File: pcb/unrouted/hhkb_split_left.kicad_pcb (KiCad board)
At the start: 4 copper layers, 140.4 x 97.4 mm, 67 parts, among them SW1 Esc, SW10 E, SW11 R, SW12 T, SW13 Ctrl, SW14 A, SW15 S, SW16 D, SW17 F, SW18 G, SW19 Shift, SW2 1, SW20 Z, SW21 X, SW22 C, SW23 V, SW24 B, SW25 Alt, SW26 Meta, SW27 L-Space, SW3 2, SW4 3, SW5 4, SW6 5, SW7 Tab, SW8 Q, SW9 W, U1 74HC595

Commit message: スイッチ→ダイオードを自分で引き、ビアを 4〜5 割減らした
自動配線器が数 mm の接続のために内層へ往復し、SW*_D だけで左 30 個・
右 62 個のビアを使っていた（右が多いのは列のバスが 9 本あって裏面が
混むため）。ソケットの端子とダイオードのアノードは同じ x に並べてあり
（DIODE_OFFSET はそのために選んだ値）、裏面の L 字 2 本で届く。
**経路に選択の余地が無い**ので prewire_switch_diode で自分で引き、
GND と同じく DSN からネットごと外して (type protect) で渡す。

  ビア 左 68→40 / 右 111→51   総長 左 1574→1538 / 右 1940→1902mm
  左右の比 1.28 がキー数の比 1.26 とほぼ一致し、非対称が規模差だけで
  説明できるようになった。DRC は 0/0 のまま

FFC が子基板まで届くかの検査を足した。J_DB を左 9.1mm・右 8.5mm
動かしたのに、それを見る検査が無かった（ケーブルは発注品なので、
合わないと分かるのが組み立て時になる）。左 92.1mm / 右 78.5mm 要り、
100mm で足りる。FFC_LENGTH / FFC_SLACK は暫定値として登録。
左右で同じケーブルが使えることも見る（部品表を 2 種類にしない）。

検査を書く途中で test_pcb.footprints() が信用できないと分かった。
`.*?` で最初の (at ...) を拾うため、J_DB では左が誤った座標・右が空を
返す。この検査では括弧の対応で切り出す _footprint_blocks を使った。

Co-Authored-By: Claude Opus 5 <noreply@anthropic.com>
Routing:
- net SW4_D: track 0.00 -> 6.89 mm
- net SW22_D: track 0.00 -> 6.89 mm
- net SW6_D: track 0.00 -> 6.89 mm
- net SW5_D: track 0.00 -> 6.89 mm
- net SW3_D: track 0.00 -> 6.89 mm
- net SW2_D: track 0.00 -> 6.89 mm
- net SW1_D: track 0.00 -> 6.89 mm
- net SW9_D: track 0.00 -> 6.89 mm
- net SW8_D: track 0.00 -> 6.89 mm
- net SW7_D: track 0.00 -> 6.89 mm
- net SW24_D: track 0.00 -> 6.89 mm
- net SW23_D: track 0.00 -> 6.89 mm
- net SW21_D: track 0.00 -> 6.89 mm
- net SW20_D: track 0.00 -> 6.89 mm
- net SW19_D: track 0.00 -> 6.89 mm
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
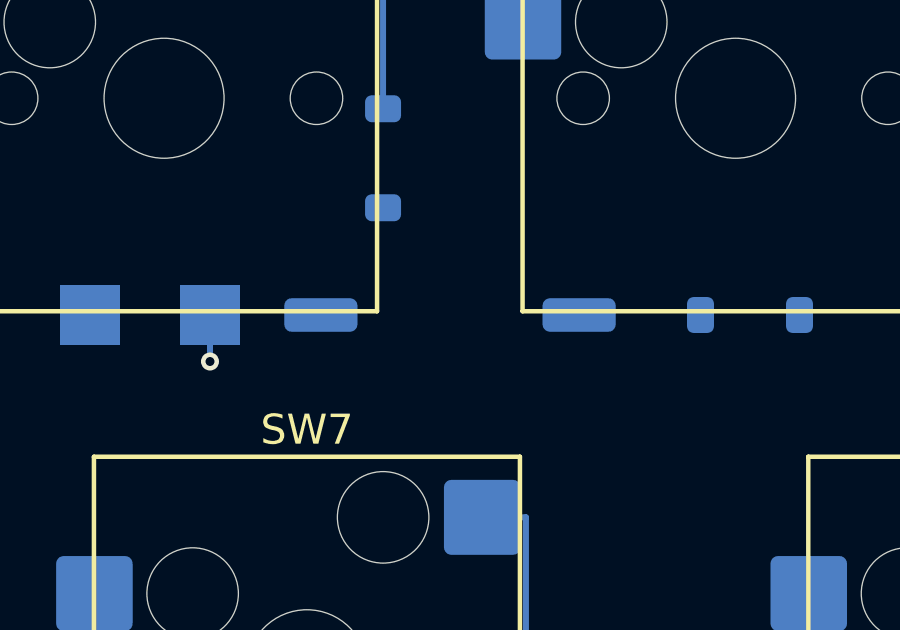
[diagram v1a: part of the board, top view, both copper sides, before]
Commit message: 電源スイッチを基板から外し、背面パネルへ（open-gaps #17 解決）
基板の後端からケース背面まで 23.3mm あり、基板の上のどこに置いても
背面には出せない。「基板に載せる」という前提自体が誤りだった。

SW_PWR の種類を wire_pads にし、基板は SW_PWR_1 / SW_PWR_2 の
ランド 2 個で受ける。電池ボックスと同じ形。実物は背面パネルに付けて
配線で繋ぐ。部品はプッシュロック（オルタネート）の丸ボタン
（実機の「電源／Bluetooth ペアリング」も丸ボタン。機械接点なので
電池を本当に切り離せる）。

再発防止に test_no_user_operated_part_is_sealed_inside を追加。
故意にスイッチを基板へ戻すと落ちることを確認済み。**最初に書いた版は
空振りしていた**（配線済み基板を読むのに再生成しか走らせておらず、
検査対象が変わっていなかった）。配線まで通して確かめ直した。

ランド 2 個への展開規則を circuit.board_refs に一本化した。
gen_pcb と test_pcb と test_conformance が別々に「battery_holder だけ
2 個」と持っていたため、電源スイッチを変えた瞬間に検査 6 件が落ちた。

検査 260 件通過。DRC は 3 基板とも 0/0 のまま。

Co-Authored-By: Claude Opus 5 <noreply@anthropic.com>
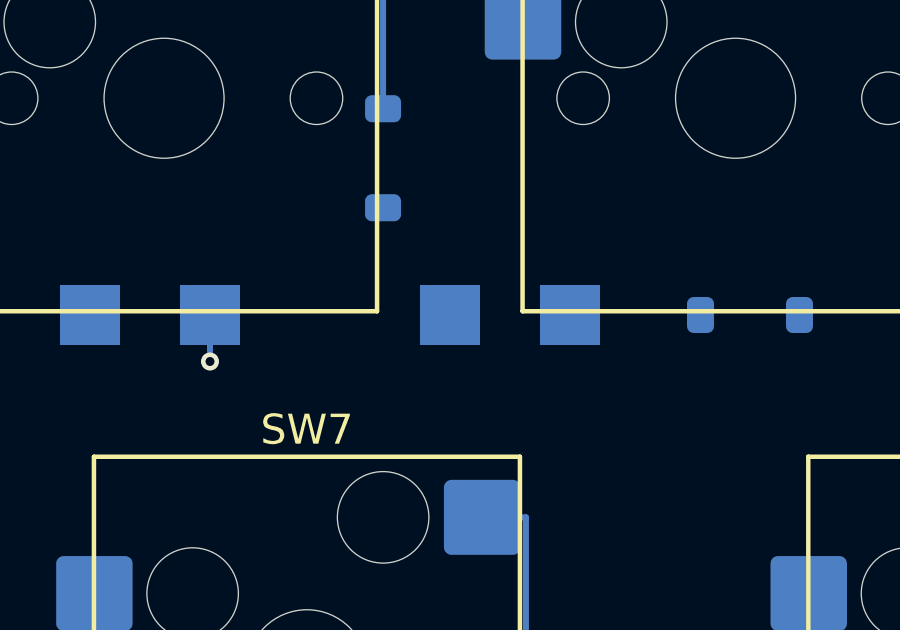
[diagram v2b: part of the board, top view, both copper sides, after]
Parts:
- removed SW_PWR: slide_switch, SW_DIP_SPSTx01_Slide_9.78x4.72mm_W8.61mm_P2.54mm
- added SW_PWR_1: wire_pads, TestPoint_Pad_2.0x2.0mm, B.Cu at (100.0, 69.1)
- added SW_PWR_2: wire_pads, TestPoint_Pad_2.0x2.0mm, B.Cu at (104.0, 69.1)

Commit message: マトリクスのダイオードを SD103AW にした（打ち止めが保証値で決まる）
1N4148W は **1mA 未満の Vf 最大値を規定していない**。行に届くのは
（レール − Vf）で nRF52840 の VIH は 0.7×レール、つまり レール ≧ Vf/0.3。
1mA の最大 0.715V で詰めるとレール 2.55V（1.48V/本）が必要になり、
**打ち止めが 1.12〜1.48V/本 の間で不定だった。電池が減るとキーが
反応しなくなる。**

SD103AW（C130875）は **VF ≦ 0.37V @ 20mA を保証**している。実使用は
100µA でそれよりはるかに小さい。必要なレールは 1.40V で、マイコンの
1.80V の内側。**打ち止めはマイコン律速の 1.10V/本 に戻った。実測不要。**

  逆漏れ 5µA @ 30V（実使用 2V ではさらに小さい）。プルダウン 13kΩ に対し
  誤検出には 20 個以上の同時押しが要る
  フットプリントは同じ SOD-123。**基板は変わらない**（Value は B.Fab のみ）
  単価 $0.0116 で 1N4148W とほぼ同じ。Basic → Extended で +$3

3 基板とも DRC 0 / 未配線 0。検査 292 件。部品 8 種すべて在庫を再確認した。
C4 からダイオードの実測手順を削り、provisional-values から
MATRIX_DIODE_VF を外した（保証値になったため）。

Co-Authored-By: Claude Opus 5 (1M context) <noreply@anthropic.com>
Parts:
- D1, D10, D11, D12, D13, D14, D15, D16, D17, D18, D19, D2, D20, D21, D22, D23, D24, D25, D26, D27, D3, D4, D5, D6, D7, D8, D9: value 1N4148W -> SD103AW
- U1: value 74HC595 -> 74LVC595

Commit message: マトリクスのダイオードを 1N4148W へ戻した（SD103AW への変更は誤り）
効く parameter は 2 つあり、片方だけ見て替えたため取り替えっこになっていた。

  (a) 走査電流での Vf … 行に届くのは（レール − Vf）。レール ≧ Vf/0.3
  (b) 逆漏れ … ダイオード本来の役目（ゴースト防止）

  型番      (a) Vf の保証         (b) 逆漏れの保証    単価/305個
  1N4148W   なし(1mA で 0.715V)   25nA @ 20V          $3.57 Basic ← 採用
  SD103AW   0.37V @ 20mA          なし(30V で 5µA)    $3.54 +$3
  BAT46W    250mV @ 0.1mA         0.5µA @ 1.5V        $28.1 +$3

SD103AW は逆漏れの保証が動作点に無い。30V の 5µA を当てると、
プルダウン 13kΩ に対して **2 個同時押しでもゴーストの margin を割る**
（引き下げ 130mV に対し余裕 120mV）。**誤った文字が出る側の失敗**なので、
打ち止めが不定であることより害が大きい。

1N4148W は逆漏れが桁違いに小さく本来の役目は保証される。不定なのは
打ち止めだけで、これは「電池が早く終わる」であって誤動作ではない。

BAT46W は両方を動作点で保証する唯一の候補（VF ≦ 250mV @ 0.1mA、
IR ≦ 0.5µA @ 1.5V）。**+$24.5（¥3,700）。**実測が難しければここへ戻る。

C4 の測定手順を戻した。**1N4007 では測れない**ことを明記した（接合が
大きく Vf が低く出る）。1N4148 が無ければ測定は飛ばしてよい。

3 基板とも DRC 0 / 未配線 0。検査 292 件。

Co-Authored-By: Claude Opus 5 (1M context) <noreply@anthropic.com>
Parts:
- D1, D10, D11, D12, D13, D14, D15, D16, D17, D18, D19, D2, D20, D21, D22, D23, D24, D25, D26, D27, D3, D4, D5, D6, D7, D8, D9: value SD103AW -> 1N4148W

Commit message: マトリクスのダイオードを BAT46W にした（1N4148W はバックアップとして記録）
在庫 5,000 超の SOD-123 ショットキー 29 件、BAT47/48/49/54/85、1SS 系、
NSR、RB751、PMEG、MBR05xx、SS12、1N5711、BAS40 を当たった。
**VF と IR を両方「動作点で」保証しているのは BAT46W だけ。**

  BAT46W(C54110)  VF≦0.25V@0.1mA   IR≦0.3µA@1.5V   $6.76(122個+段取り)
  1N4148W(C81598) なし(1mA 0.715V) なし(20V 25nA)  $1.43 Basic
  SD103AW         0.37V@20mA       なし(30V 5µA)   $6.75
  BAT54W          240mV@0.1mA      なし(25V 2µA)   $6.25

罠: BAT48ZFILM-FS(C7436546) は名前だけで中身は SD103AW と同じ仕様。

## 効果

打ち止めがマイコン律速に戻る（1.20 → **1.10V/本**）。
**壊れ方が「一部のキーが反応しない」から「電源が落ちる」に変わる。**
実測が不要になる。

## 代償（数字で押さえた）

+約 ¥800。逆漏れ 12 倍で **60℃ かつ 5 個以上の同時押しだと余裕を割る**
（25℃ なら 9 個でも OK）。接合容量 5 倍だが列切替後 2.31µs に対し
SPI 転送で 4.0µs 以上空くので間に合う。

## 検査を 2 つ足した

  test_the_matrix_reads_high_at_the_cutoff … 打ち止めで行が VIH に届くか
  test_ghosting_survives_a_full_row_of_simultaneous_presses … 逆漏れの合計

どちらも故意に壊して検出を確認した。**1 回目は __pycache__ が古いまま
（同じ秒に書き換えたため）で検出できていなかった。**破壊試験のあとは
バイトコードを消すこと。

open-gaps #25 に「電池が尽きるときの止まり方」を記録した。マイコンの
ブラウンアウトは起動と広告を繰り返しうるし、**低電圧の flash 書き込みで
ペアリング情報が壊れうる**。POFCON か soft-off で自分から止めれば直るが、
ZMK に機能が無いので自作が要る。**基板に影響しないので届いてからでよい。**

3 基板とも DRC 0 / 未配線 0。検査 294 件。

Co-Authored-By: Claude Opus 5 (1M context) <noreply@anthropic.com>
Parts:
- D1, D10, D11, D12, D13, D14, D15, D16, D17, D18, D19, D2, D20, D21, D22, D23, D24, D25, D26, D27, D3, D4, D5, D6, D7, D8, D9: value 1N4148W -> BAT46W

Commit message: #23 の D9 移設を実施した（アンテナ実外形の真下の配線が 0 本になった）
- ROW4 の行き先を D5（左列）→ D9（右列・元 MISO）へ。TX 側レーン 6 → 5 本、
  LANE_STEP 0.7 → 0.65。最内レーン -3.8mm はアンテナ実外形（-3.65〜-0.15）の外
- ケーブルのピン配置は ROW4 を右群 4 番へ（左群のままだと横枝が縦線を
  8 箇所で横切る。DRC で実測）。本体基板 2 枚も再生成＋再配線。3 基板 DRC 0
- ファームは row-gpios を D9 へ、&spi2_default/&spi2_sleep の psels から
  MISO を外して P1.14 を解放（CI ビルド・実機は未確認）
- 買い物リストを shopping-list.md に統合（#22 の再発防止の作法つき）
- Task C3 §6-6b に測定条件欄を追加
- 全検査 386 passed / 3 skipped

Co-Authored-By: Claude Fable 5 <noreply@anthropic.com>
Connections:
- J_DB pad 10: ROW3 -> ROW2
- J_DB pad 11: ROW4 -> ROW3
- J_DB pad 4: SPI_MOSI -> ROW4
- J_DB pad 5: V3V3 -> SPI_MOSI
- J_DB pad 6: VBATT_SENSE -> V3V3
- J_DB pad 7: ROW0 -> VBATT_SENSE
- J_DB pad 8: ROW1 -> ROW0
- J_DB pad 9: ROW2 -> ROW1
